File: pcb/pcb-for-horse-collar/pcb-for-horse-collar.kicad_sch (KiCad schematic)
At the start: 4 parts, among them U1 ESP32-WROOM-32E, U2 BNO085, U3 CP2102N-Axx-xQFN20, U4 MCP73831-2-OT

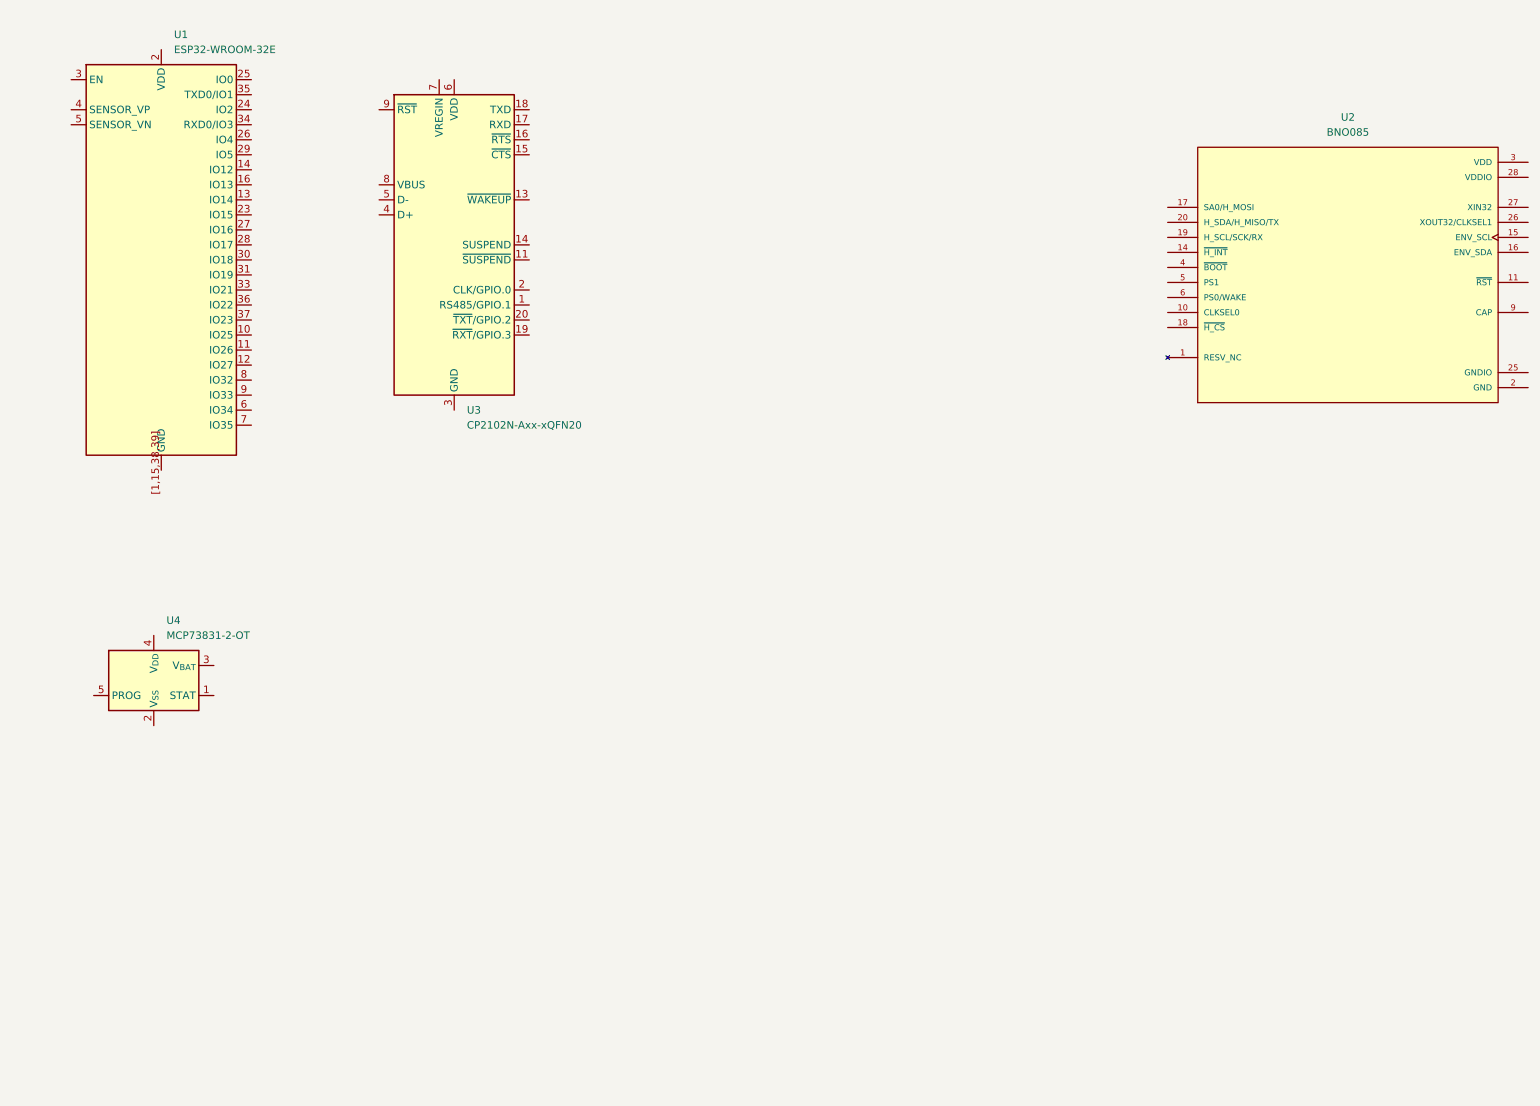
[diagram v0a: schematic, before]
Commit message: Add wirings and nets to schematics.
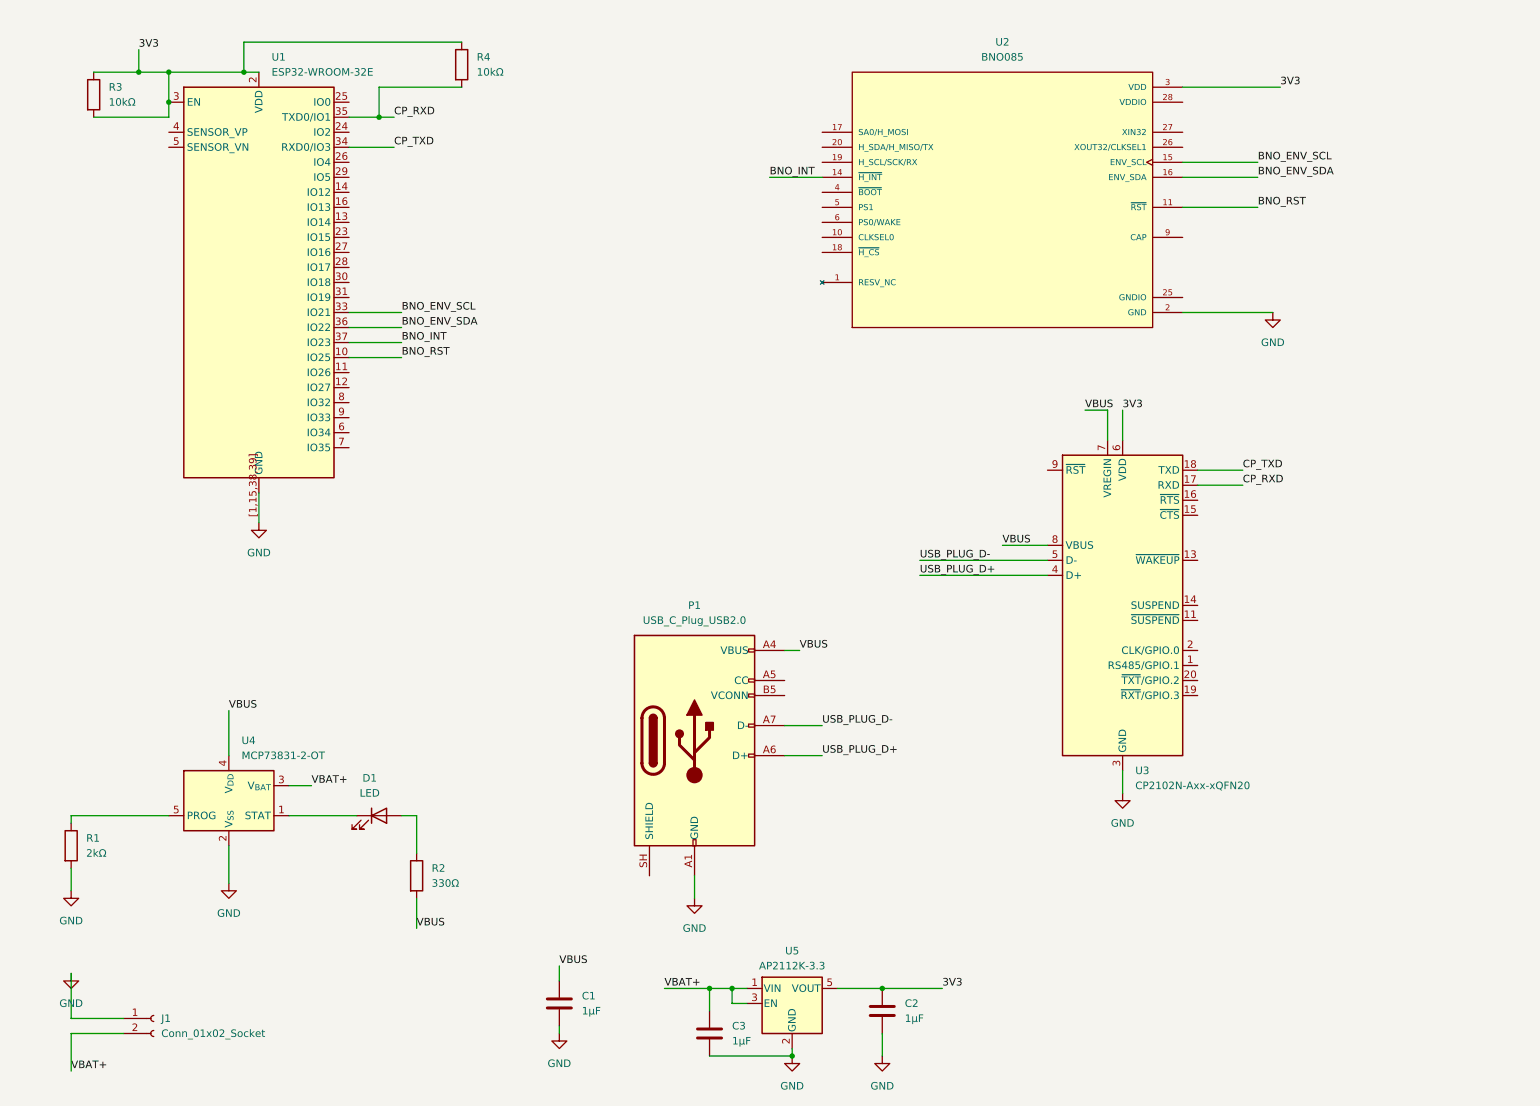
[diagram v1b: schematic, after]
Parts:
- added C1, C2, C3: 1µF, symbol Device:C
- added D1: LED, symbol Device:LED
- added J1: Conn_01x02_Socket, symbol Connector:Conn_01x02_Socket
- added P1: USB_C_Plug_USB2.0, symbol Connector:USB_C_Plug_USB2.0
- added R1: 2kΩ, symbol Device:R
- added R2: 330Ω, symbol Device:R
- added R3, R4: 10kΩ, symbol Device:R
- added U5: AP2112K-3.3, Package_TO_SOT_SMD:SOT-23-5, symbol Regulator_Linear:AP2112K-3.3
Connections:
- net at U4.1 (STAT): now also D1.1 (K)
- net GND: now reaches U4.2 (V_{SS})
- net GND: now also U1.[1,15,38,39] (GND), U2.2 (GND), U3.12 (GND), U3.21 (GND), U3.3 (GND), C1.2, C2.2, C3.2, J1.1 (Pin_1), P1.A1 (GND), P1.A12 (GND), P1.B1 (GND), P1.B12 (GND), R1.2, U5.2 (GND)
- net VBAT+: now reaches U4.3 (V_{BAT})
- net VBAT+: now also C3.1, J1.2 (Pin_2), U5.1 (VIN), U5.3 (EN)
- net VBUS: now reaches U4.4 (V_{DD})
- net VBUS: now also U3.7 (VREGIN), U3.8 (VBUS), C1.1, P1.A4 (VBUS), P1.A9 (VBUS), P1.B4 (VBUS), P1.B9 (VBUS), R2.2
- net at U4.5 (PROG): now also R1.1
- net BNO_RST: now reaches U2.11 (~{RST})
- net BNO_RST: now also U1.10 (IO25)
- net BNO_INT: now reaches U2.14 (~{H_INT})
- net BNO_INT: now also U1.37 (IO23)
- net BNO_ENV_SCL: now reaches U2.15 (ENV_SCL)
- net BNO_ENV_SCL: now also U1.33 (IO21)
- net BNO_ENV_SDA: now reaches U2.16 (ENV_SDA)
- net BNO_ENV_SDA: now also U1.36 (IO22)
- net 3V3: now reaches U2.3 (VDD)
- net 3V3: now also U1.2 (VDD), U1.3 (EN), U3.6 (VDD), C2.1, R3.1, R3.2, R4.1, U5.5 (VOUT)
- net CP_RXD: now reaches U3.17 (RXD)
- net CP_RXD: now also U1.35 (TXD0/IO1), R4.2
- net CP_TXD: now reaches U3.18 (TXD)
- net CP_TXD: now also U1.34 (RXD0/IO3)
- net USB_PLUG_D+: now reaches U3.4 (D+)
- net USB_PLUG_D+: now also P1.A6 (D+)
- net USB_PLUG_D-: now reaches U3.5 (D-)
- net USB_PLUG_D-: now also P1.A7 (D-)
- new net: D1.2 (A), R2.1
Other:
- moved on the sheet: U1, U2, U3, U4

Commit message: Update schematics
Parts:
- added C4, C6: 100nF, symbol Device:C
- added C5: 4.7µF, symbol Device:C
- added Q1, Q2: S8050, Package_TO_SOT_THT:TO-92_Inline, symbol Transistor_BJT:S8050
- added R5: 5.1 kΩ, symbol Device:R
- added R6, R7: 10 kΩ, symbol Device:R
- added R8: 4.7 kΩ, symbol Device:R
- R3: value 10kΩ -> 10 kΩ
- R4: value 10kΩ -> 4.7 kΩ
- U3: value CP2102N-Axx-xQFN20 -> CP2102N-Axx-xQFN28; footprint Package_DFN_QFN:SiliconLabs_QFN-20-1EP_3x3mm_P0.5mm -> Package_DFN_QFN:QFN-28-1EP_5x5mm_P0.5mm_EP3.35x3.35mm; symbol Interface_USB:CP2102N-Axx-xQFN20 -> Interface_USB:CP2102N-Axx-xQFN28
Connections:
- net 3V3: now also R4.2, U2.18 (~{H_CS}), U2.28 (VDDIO), R8.2; no longer R3.2, R4.1, U1.3 (EN), U3.6 (VDD)
- net CP_RXD: now also U3.25 (RXD); no longer R4.2, U3.17 (RXD)
- net CP_TXD: now also U3.26 (TXD); no longer U3.18 (TXD)
- net GND: now also U2.17 (SA0/H_MOSI), U2.25 (GNDIO), U2.5 (PS1), U2.6 (PS0/WAKE), U3.29 (GND), C4.1, C5.1, C6.2, R5.2; no longer U3.12 (GND), U3.21 (GND)
- net BNO_H_SCL: now reaches U2.19 (H_SCL/SCK/RX)
- net BNO_H_SCL: now also R4.1, U1.33 (IO21)
- net BNO_H_SDA: now reaches U2.20 (H_SDA/H_MISO/TX)
- net BNO_H_SDA: now also U1.36 (IO22), R8.1
- net at U2.9 (CAP): now also C6.1
- net at P1.A5 (CC): now also R5.1
- net Q2_Collector: now reaches U1.25 (IO0)
- net Q2_Collector: now also Q2.3 (C)
- net BNO_ENV_SCL: no longer names the net of U2.15 (ENV_SCL)
- net BNO_ENV_SCL: no longer U1.33 (IO21)
- net BNO_ENV_SDA: no longer names the net of U2.16 (ENV_SDA)
- net BNO_ENV_SDA: no longer U1.36 (IO22)
- new net: Q2.2 (B), R7.2
- new net: C5.2, U3.6 (VDD)
- new net: Q1.2 (B), R6.2
- new net CP_DTR: Q2.1 (E), R6.1, U3.28 (~{DTR})
- new net CP_RTS: Q1.1 (E), R7.1, U3.24 (~{RTS})
- new net Q1_Collector: C4.2, Q1.3 (C), R3.2, U1.3 (EN)
- no-connect marks 0 -> 45
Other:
- moved on the sheet: D1, R2, U2

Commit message: WIP: Working on pcb.
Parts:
- C1, C2, C3, C4, C5, C6: footprint (none) -> Capacitor_SMD:C_0805_2012Metric
- D1: footprint (none) -> LED_SMD:LED_0805_2012Metric
- J1: footprint (none) -> Connector_PinSocket_2.54mm:PinSocket_1x02_P2.54mm_Vertical
- P1: footprint (none) -> Connector_USB:USB_C_Plug_ShenzhenJingTuoJin_918-118A2021Y40002_Vertical
- R1, R2, R3, R4, R5, R6, R7, R8: footprint (none) -> Resistor_SMD:R_0805_2012Metric
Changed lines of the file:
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@@
 			)
 		)
-		(property "Footprint" ""
+		(property "Footprint" "Resistor_SMD:R_0805_2012Metric"
 			(at 156.21 33.528 90)
 			(hide yes)
@@
 			)
 		)
-		(property "Footprint" ""
+		(property "Footprint" "Resistor_SMD:R_0805_2012Metric"
 			(at 69.342 163.83 90)
 			(hide yes)
@@
 			)
 		)
-		(property "Footprint" ""
+		(property "Footprint" "Resistor_SMD:R_0805_2012Metric"
 			(at 165.862 129.54 90)
 			(hide yes)
@@
 			)
 		)
-		(property "Footprint" ""
+		(property "Footprint" "Capacitor_SMD:C_0805_2012Metric"
 			(at 31.75 37.1348 0)
 			(hide yes)
@@
 			)
 		)
-		(property "Footprint" ""
+		(property "Footprint" "Resistor_SMD:R_0805_2012Metric"
 			(at 156.21 46.228 90)
 			(hide yes)
@@
 			)
 		)
-		(property "Footprint" ""
+		(property "Footprint" "Capacitor_SMD:C_0805_2012Metric"
 			(at 251.46 52.3748 0)
 			(hide yes)
@@
 			)
 		)
-		(property "Footprint" ""
+		(property "Footprint" "Capacitor_SMD:C_0805_2012Metric"
 			(at 131.7752 189.23 0)
 			(hide yes)
@@
 			)
 		)
-		(property "Footprint" ""
+		(property "Footprint" "LED_SMD:LED_0805_2012Metric"
 			(at 74.93 156.21 0)
 			(hide yes)
@@
 			)
 		)
-		(property "Footprint" ""
+		(property "Footprint" "Capacitor_SMD:C_0805_2012Metric"
 			(at 106.3752 184.15 0)
 			(hide yes)
@@
 			)
 		)
-		(property "Footprint" ""
+		(property "Footprint" "Resistor_SMD:R_0805_2012Metric"
 			(at 21.082 153.67 90)
 			(hide yes)
@@
 			)
 		)
-		(property "Footprint" ""
+		(property "Footprint" "Connector_USB:USB_C_Plug_ShenzhenJingTuoJin_918-118A2021Y40002_Vertical"
 			(at 132.08 135.89 0)
 			(hide yes)
@@
 			)
 		)
-		(property "Footprint" ""
+		(property "Footprint" "Capacitor_SMD:C_0805_2012Metric"
 			(at 160.9852 185.42 0)
 			(hide yes)
@@
 			)
 		)
-		(property "Footprint" ""
+		(property "Footprint" "Capacitor_SMD:C_0805_2012Metric"
 			(at 206.7052 78.74 0)
 			(hide yes)
@@
 			)
 		)
-		(property "Footprint" ""
+		(property "Footprint" "Connector_PinSocket_2.54mm:PinSocket_1x02_P2.54mm_Vertical"
 			(at 36.83 182.88 0)
 			(hide yes)
@@
 			)
 		)
-		(property "Footprint" ""
+		(property "Footprint" "Resistor_SMD:R_0805_2012Metric"
 			(at 29.21 22.098 90)
 			(hide yes)
@@
 			)
 		)
-		(property "Footprint" ""
+		(property "Footprint" "Resistor_SMD:R_0805_2012Metric"
 			(at 111.76 61.468 90)
 			(hide yes)
@@
 			)
 		)
-		(property "Footprint" ""
+		(property "Footprint" "Resistor_SMD:R_0805_2012Metric"
 			(at 111.76 33.528 90)
 			(hide yes)

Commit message: WIP: About to add mosfet for charging and switch to turn it on and off.
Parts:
- added R10: 5.1 kΩ, Resistor_SMD:R_0805_2012Metric, symbol Device:R
- added R9: 10 kΩ, Resistor_SMD:R_0805_2012Metric, symbol Device:R
- J1: footprint Connector_PinSocket_2.54mm:PinSocket_1x02_P2.54mm_Vertical -> Connector_JST:JST_PH_B2B-PH-K_1x02_P2.00mm_Vertical
- P1: value USB_C_Plug_USB2.0 -> USB_C_Receptacle_USB2.0_16P; footprint Connector_USB:USB_C_Plug_ShenzhenJingTuoJin_918-118A2021Y40002_Vertical -> Connector_USB:USB_C_Receptacle_GCT_USB4105-xx-A_16P_TopMnt_Horizontal; symbol Connector:USB_C_Plug_USB2.0 -> Connector:USB_C_Receptacle_USB2.0_16P
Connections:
- net 3V3: now also R4.1, R9.2; no longer R4.2
- net BNO_H_SCL: now also R4.2; no longer R4.1
- net GND: now also U2.10 (CLKSEL0), R10.2
- net VBUS: now also D1.2 (A); no longer R2.2
- net at U4.1 (STAT): now also R2.1; no longer D1.1 (K)
- net at U2.4 (~{BOOT}): now also R9.1
- net at P1.B5 (CC2): now also R10.1
- new net: D1.1 (K), R2.2
- no-connect marks 45 -> 46
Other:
- moved on the sheet: R2, R4, R5

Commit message: Adding switch.
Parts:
- added SW1: SW_SPST, Button_Switch_SMD:SW_DIP_SPSTx01_Slide_6.7x4.1mm_W6.73mm_P2.54mm_LowProfile_JPin, symbol Switch:SW_SPST
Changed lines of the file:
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@@
+	)
+	(symbol
+		(lib_id "Switch:SW_SPST")
+		(at 87.63 118.11 0)
+		(unit 1)
+		(body_style 1)
+		(exclude_from_sim no)
+		(in_bom yes)
+		(on_board yes)
+		(in_pos_files yes)
+		(dnp no)
+		(fields_autoplaced yes)
+		(property "Reference" "SW1"
+			(at 87.63 111.76 0)
+			(show_name no)
+			(do_not_autoplace no)
+			(effects
+				(font
+					(size 1.27 1.27)
+				)
+			)
+		)
+		(property "Value" "SW_SPST"
+			(at 87.63 114.3 0)
+			(show_name no)
+			(do_not_autoplace no)
+			(effects
+				(font
+					(size 1.27 1.27)
+				)
+			)
+		)
+		(property "Footprint" "Button_Switch_SMD:SW_DIP_SPSTx01_Slide_6.7x4.1mm_W6.73mm_P2.54mm_LowProfile_JPin"
+			(at 87.63 118.11 0)
+			(hide yes)
+			(show_name no)
+			(do_not_autoplace no)
+			(effects
+				(font
+					(size 1.27 1.27)
+				)
+			)
+		)
+		(property "Datasheet" ""
+			(at 87.63 118.11 0)
+			(hide yes)
+			(show_name no)
+			(do_not_autoplace no)
+			(effects
+				(font
+					(size 1.27 1.27)
+				)
+			)
+		)
+		(property "Description" "Single Pole Single Throw (SPST) switch"
+			(at 87.63 118.11 0)
+			(hide yes)
+			(show_name no)
+			(do_not_autoplace no)
+			(effects
+				(font
+					(size 1.27 1.27)
+				)
+			)
+		)
+		(pin "1"
+		)
+		(pin "2"
+		)
+		(instances
+			(project "pcb-for-horse-collar"
+				(path "/f4a125dd-bdad-4662-a165-3e2bf8c8462c"
+					(reference "SW1")
+					(unit 1)
+				)
+			)
+		)
 	)
 	(symbol
